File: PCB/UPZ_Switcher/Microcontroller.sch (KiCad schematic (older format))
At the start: 9 parts, among them IC1 MAX232ECPE+, J1 5747844-6

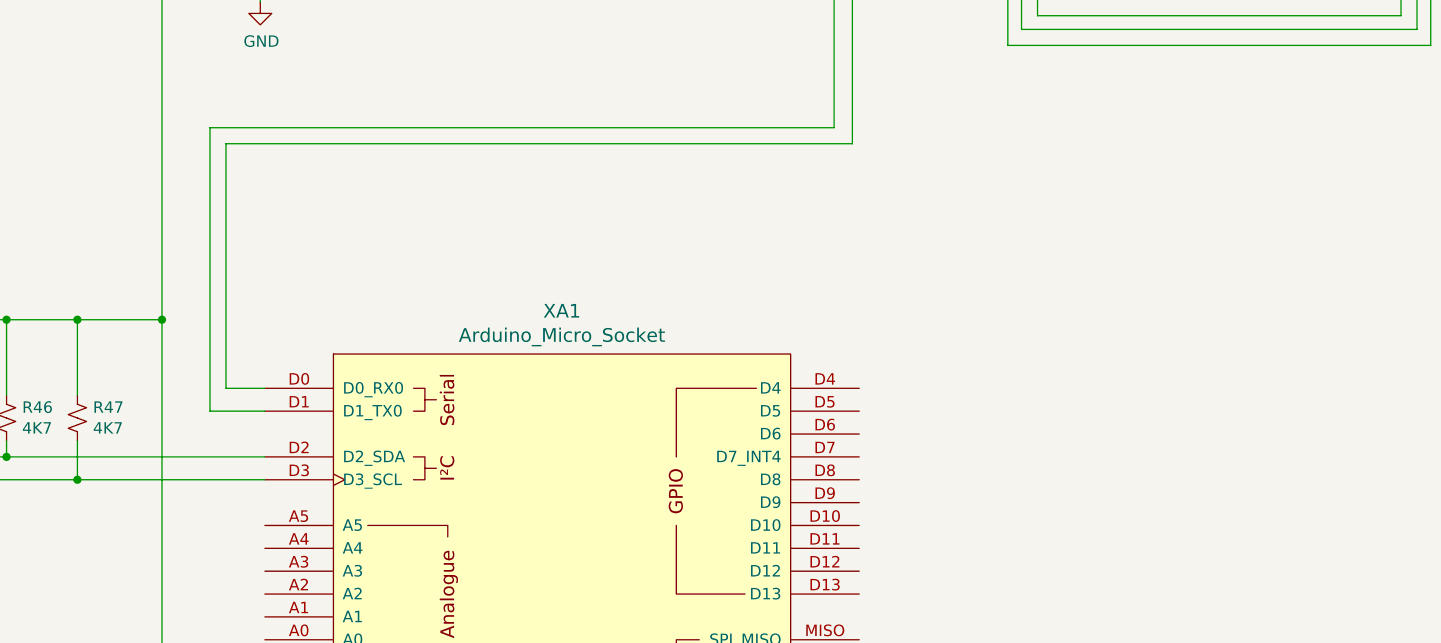
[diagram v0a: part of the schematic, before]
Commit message: Updated schematic, PSU added + draft program
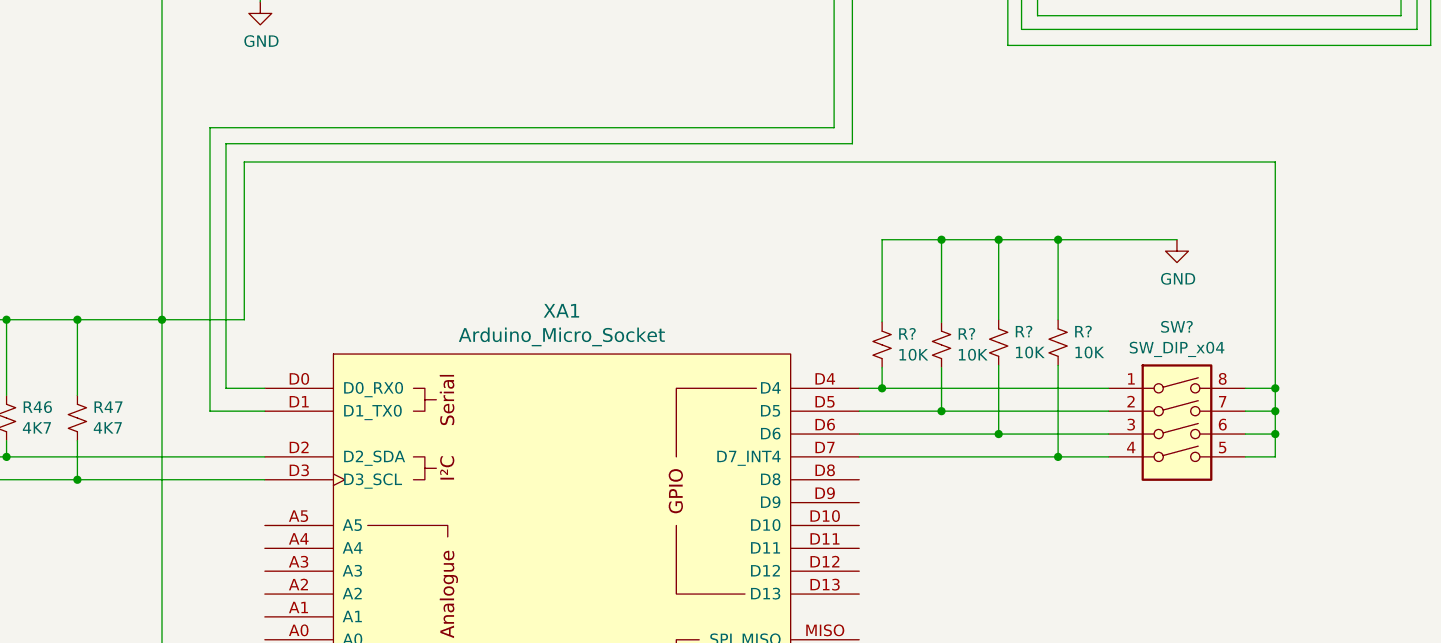
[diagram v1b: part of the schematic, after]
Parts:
- added R? (x4): 10K, Resistor_SMD:R_1206_3216Metric, symbol Device:R_Small_US
- added SW?: SW_DIP_x04, Button_Switch_THT:SW_DIP_SPSTx04_Slide_9.78x12.34mm_W7.62mm_P2.54mm, symbol Switch:SW_DIP_x04
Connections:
- wire segments 68 -> 99
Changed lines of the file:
@@
 $Descr A3 16535 11693
 encoding utf-8
-Sheet 3 6
+Sheet 3 5
 Title "Microcontroller Board"
 Date "2021-02-28"
@@
 Wire Wire Line
 	10450 1540 10590 1540
+$Comp
+L Switch:SW_DIP_x04 SW?
+U 1 1 603D5AFB
+P 10800 4200
+F 0 "SW?" H 10800 4667 50  0000 C CNN
+F 1 "SW_DIP_x04" H 10800 4576 50  0000 C CNN
+F 2 "Button_Switch_THT:SW_DIP_SPSTx04_Slide_9.78x12.34mm_W7.62mm_P2.54mm" H 10800 4200 50  0001 C CNN
+F 3 "~" H 10800 4200 50  0001 C CNN
+	1    10800 4200
+	1    0    0    -1
+$EndComp
+Wire Wire Line
+	6360 3700 6720 3700
+Wire Wire Line
+	6720 3700 6720 3010
+Wire Wire Line
+	11230 4000 11100 4000
+Wire Wire Line
+	11100 4100 11230 4100
+Connection ~ 11230 4000
+Wire Wire Line
+	11100 4200 11230 4200
+Wire Wire Line
+	11230 4000 11230 4100
+Connection ~ 11230 4100
+Wire Wire Line
+	11230 4100 11230 4200
+Wire Wire Line
+	11100 4300 11230 4300
+Wire Wire Line
+	11230 4300 11230 4200
+Connection ~ 11230 4200
+Wire Wire Line
+	11230 3010 11230 4000
+$Comp
+L Device:R_Small_US R?
+U 1 1 603E88E2
+P 9510 3810
+F 0 "R?" H 9578 3856 50  0000 L CNN
+F 1 "10K" H 9578 3765 50  0000 L CNN
+F 2 "Resistor_SMD:R_1206_3216Metric" H 9510 3810 50  0001 C CNN
+F 3 "~" H 9510 3810 50  0001 C CNN
+	1    9510 3810
+	1    0    0    -1
+$EndComp
+$Comp
+L Device:R_Small_US R?
+U 1 1 603EE6CE
+P 9770 3810
+F 0 "R?" H 9838 3856 50  0000 L CNN
+F 1 "10K" H 9838 3765 50  0000 L CNN
+F 2 "Resistor_SMD:R_1206_3216Metric" H 9770 3810 50  0001 C CNN
+F 3 "~" H 9770 3810 50  0001 C CNN
+	1    9770 3810
+	1    0    0    -1
+$EndComp
+$Comp
+L Device:R_Small_US R?
+U 1 1 603FFE72
+P 10020 3800
+F 0 "R?" H 10088 3846 50  0000 L CNN
+F 1 "10K" H 10088 3755 50  0000 L CNN
+F 2 "Resistor_SMD:R_1206_3216Metric" H 10020 3800 50  0001 C CNN
+F 3 "~" H 10020 3800 50  0001 C CNN
+	1    10020 3800
+	1    0    0    -1
+$EndComp
+$Comp
+L Device:R_Small_US R?
+U 1 1 603FFE7C
+P 10280 3800
+F 0 "R?" H 10348 3846 50  0000 L CNN
+F 1 "10K" H 10348 3755 50  0000 L CNN
+F 2 "Resistor_SMD:R_1206_3216Metric" H 10280 3800 50  0001 C CNN
+F 3 "~" H 10280 3800 50  0001 C CNN
+	1    10280 3800
+	1    0    0    -1
+$EndComp
+Wire Wire Line
+	6720 3010 11230 3010
+Wire Wire Line
+	9410 4000 9510 4000
+Wire Wire Line
+	9410 4100 9770 4100
+Wire Wire Line
+	9410 4200 10020 4200
+Wire Wire Line
+	9410 4300 10280 4300
+Wire Wire Line
+	10280 3900 10280 4300
+Connection ~ 10280 4300
+Wire Wire Line
+	10280 4300 10500 4300
+Wire Wire Line
+	10020 3900 10020 4200
+Connection ~ 10020 4200
+Wire Wire Line
+	10020 4200 10500 4200
+Wire Wire Line
+	9770 3910 9770 4100
+Connection ~ 9770 4100
+Wire Wire Line
+	9770 4100 10500 4100
+Wire Wire Line
+	9510 3910 9510 4000
+Connection ~ 9510 4000
+Wire Wire Line
+	9510 4000 10500 4000
+$Comp
+L power:GND #PWR?
+U 1 1 604268ED
+P 10800 3350
+F 0 "#PWR?" H 10800 3100 50  0001 C CNN
+F 1 "GND" H 10805 3177 50  0000 C CNN
+F 2 "" H 10800 3350 50  0001 C CNN
+F 3 "" H 10800 3350 50  0001 C CNN
+	1    10800 3350
+	1    0    0    -1
+$EndComp
+Wire Wire Line
+	9510 3350 9770 3350
+Wire Wire Line
+	9510 3350 9510 3710
+Wire Wire Line
+	9770 3710 9770 3350
+Connection ~ 9770 3350
+Wire Wire Line
+	9770 3350 10020 3350
+Wire Wire Line
+	10020 3700 10020 3350
+Connection ~ 10020 3350
+Wire Wire Line
+	10020 3350 10280 3350
+Wire Wire Line
+	10280 3700 10280 3350
+Connection ~ 10280 3350
+Wire Wire Line
+	10280 3350 10800 3350
 $EndSCHEMATC

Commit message: Started PCB design
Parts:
- added R1, R2, R3: 10K, Resistor_SMD:R_1206_3216Metric, symbol Device:R_Small_US
- added R5: 20K, Resistor_SMD:R_1206_3216Metric, symbol Device:R_Small_US
- added R7: 40K, Resistor_SMD:R_1206_3216Metric, symbol Device:R_Small_US
- added R9: 80K, Resistor_SMD:R_1206_3216Metric, symbol Device:R_Small_US
- added SW1: SW_DIP_x04, Button_Switch_THT:SW_DIP_SPSTx04_Slide_9.78x12.34mm_W7.62mm_P2.54mm, symbol Switch:SW_DIP_x04
- R10: renamed from R?; value 10K -> 80K
- R6: renamed from R?; value 10K -> 20K
- R8: renamed from R?; value 10K -> 40K
- gave numbers to parts that had none: 2
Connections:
- wire segments 99 -> 122
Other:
- note added: "Input \nSwitcher \nDIP Address"
- note added: "Output \nSwitcher \nDIP Address"
- moved on the sheet: R10, R4, R6, R8, SW2

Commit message: updated phantom design + MCU board
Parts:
- removed J1: 5747844-6, 57478446, symbol BVKSound:5747844-6
- added J1: FROM PSU, BVKSound:71918-110LF, symbol BVKSound:71918-110LF
- added J2: TO RELAY, BVKSound:71918-110LF, symbol BVKSound:71918-110LF
- added J3: FROM PREVIOUS, Connector_Dsub:DSUB-9_Female_Horizontal_P2.77x2.84mm_EdgePinOffset4.94mm_Housed_MountingHolesOffset7.48mm, symbol Connector:DB9_Female
- added J4: TO NEXT, Connector_Dsub:DSUB-9_Male_Horizontal_P2.77x2.84mm_EdgePinOffset4.94mm_Housed_MountingHolesOffset7.48mm, symbol Connector:DB9_Male
- C19, C20, C21, C22: footprint (none) -> Capacitor_THT:CP_Radial_D5.0mm_P2.50mm
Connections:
- wire segments 122 -> 146
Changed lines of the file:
@@
 $Descr A3 16535 11693
 encoding utf-8
-Sheet 1 6
+Sheet 1 1
 Title "Microcontroller Board"
 Date "2021-02-28"
@@
 	1    0    0    -1
 $EndComp
-$Comp
-L BVKSound:5747844-6 J1
-U 1 1 63464424
-P 11090 1140
-F 0 "J1" V 10909 1140 50  0000 C CNN
-F 1 "5747844-6" V 11000 1140 50  0000 C CNN
-F 2 "57478446" H 11940 1440 50  0001 L CNN
-F 3 "http://www.te.com/commerce/DocumentDelivery/DDEController?Action=showdoc&DocId=Customer+Drawing%7F5747844%7FP%7Fpdf%7FEnglish%7FENG_CD_5747844_P.pdf%7F5747844-6" H 11940 1340 50  0001 L CNN
-F 4 "9 way r/a PCB D socket w/screw lock,6A" H 11940 1240 50  0001 L CNN "Description"
-F 5 "12" H 11940 1140 50  0001 L CNN "Height"
-F 6 "TE Connectivity" H 11940 1040 50  0001 L CNN "Manufacturer_Name"
-F 7 "5747844-6" H 11940 940 50  0001 L CNN "Manufacturer_Part_Number"
-F 8 "571-5747844-6" H 11940 840 50  0001 L CNN "Mouser Part Number"
-F 9 "https://www.mouser.co.uk/ProductDetail/TE-Connectivity/5747844-6?qs=x6EjVpvqMVNBaI3EeeZZVw%3D%3D" H 11940 740 50  0001 L CNN "Mouser Price/Stock"
-F 10 "5747844-6" H 11940 640 50  0001 L CNN "Arrow Part Number"
-F 11 "https://www.arrow.com/en/products/5747844-6/te-connectivity" H 11940 540 50  0001 L CNN "Arrow Price/Stock"
-	1    11090 1140
-	0    1    1    0
-$EndComp
 Wire Wire Line
 	8790 1680 10120 1680
 Wire Wire Line
 	10120 1680 10120 2430
-Wire Wire Line
-	10120 2430 11850 2430
-Wire Wire Line
-	11850 2430 11850 1740
-Wire Wire Line
-	11850 1740 11590 1740
-Wire Wire Line
-	11590 1640 11910 1640
-Wire Wire Line
-	11910 1640 11910 2500
-Wire Wire Line
-	11910 2500 10060 2500
 Wire Wire Line
 	10060 2500 10060 1780
@@
 F 0 "C19" H 6878 1626 50  0000 L CNN
 F 1 "1uF" H 6878 1535 50  0000 L CNN
-F 2 "" H 6790 1580 50  0001 C CNN
+F 2 "Capacitor_THT:CP_Radial_D5.0mm_P2.50mm" H 6790 1580 50  0001 C CNN
 F 3 "~" H 6790 1580 50  0001 C CNN
 	1    6790 1580
@@
 F 0 "C22" H 7338 1336 50  0000 L CNN
 F 1 "1uF" H 7338 1245 50  0000 L CNN
-F 2 "" H 7250 1290 50  0001 C CNN
+F 2 "Capacitor_THT:CP_Radial_D5.0mm_P2.50mm" H 7250 1290 50  0001 C CNN
 F 3 "~" H 7250 1290 50  0001 C CNN
 	1    7250 1290
@@
 F 0 "C20" H 6878 1926 50  0000 L CNN
 F 1 "1uF" H 6878 1835 50  0000 L CNN
-F 2 "" H 6790 1880 50  0001 C CNN
+F 2 "Capacitor_THT:CP_Radial_D5.0mm_P2.50mm" H 6790 1880 50  0001 C CNN
 F 3 "~" H 6790 1880 50  0001 C CNN
 	1    6790 1880
@@
 F 0 "C21" H 6702 2114 50  0000 R CNN
 F 1 "1uF" H 6702 2205 50  0000 R CNN
-F 2 "" H 6790 2160 50  0001 C CNN
+F 2 "Capacitor_THT:CP_Radial_D5.0mm_P2.50mm" H 6790 2160 50  0001 C CNN
 F 3 "~" H 6790 2160 50  0001 C CNN
 	1    6790 2160
@@
 Wire Wire Line
 	6790 2310 6790 2260
-$Comp
-L power:GND #PWR0126
-U 1 1 6348982D
-P 12220 1440
-F 0 "#PWR0126" H 12220 1190 50  0001 C CNN
-F 1 "GND" H 12225 1267 50  0000 C CNN
-F 2 "" H 12220 1440 50  0001 C CNN
-F 3 "" H 12220 1440 50  0001 C CNN
-	1    12220 1440
-	1    0    0    -1
-$EndComp
-Wire Wire Line
-	11590 1440 12220 1440
-Wire Wire Line
-	11590 1540 11780 1540
-Wire Wire Line
-	11780 1540 11780 2370
-Wire Wire Line
-	11780 2370 10190 2370
-Wire Wire Line
-	10190 2370 10190 1740
-Wire Wire Line
-	10190 1740 10590 1740
-Wire Wire Line
-	10590 1640 10450 1640
-Wire Wire Line
-	10450 1640 10450 1540
-Wire Wire Line
-	10450 1540 10590 1540
 $Comp
 L Switch:SW_DIP_x04 SW2
@@
 Wire Wire Line
 	8790 1980 9820 1980
+$Comp
+L Connector:DB9_Female J3
+U 1 1 604F5662
+P 11240 3140
+F 0 "J3" H 11420 3186 50  0000 L CNN
+F 1 "FROM PREVIOUS" H 11420 3095 50  0000 L CNN
+F 2 "Connector_Dsub:DSUB-9_Female_Horizontal_P2.77x2.84mm_EdgePinOffset4.94mm_Housed_MountingHolesOffset7.48mm" H 11240 3140 50  0001 C CNN
+F 3 " ~" H 11240 3140 50  0001 C CNN
+	1    11240 3140
+	1    0    0    -1
+$EndComp
+$Comp
+L Connector:DB9_Male J4
+U 1 1 604F7554
+P 13410 3100
+F 0 "J4" H 13590 3146 50  0000 L CNN
+F 1 "TO NEXT" H 13590 3055 50  0000 L CNN
+F 2 "Connector_Dsub:DSUB-9_Male_Horizontal_P2.77x2.84mm_EdgePinOffset4.94mm_Housed_MountingHolesOffset7.48mm" H 13410 3100 50  0001 C CNN
+F 3 " ~" H 13410 3100 50  0001 C CNN
+	1    13410 3100
+	1    0    0    -1
+$EndComp
+Wire Wire Line
+	10940 3040 10860 3040
+Wire Wire Line
+	10860 3040 10860 3240
+Wire Wire Line
+	10860 3240 10940 3240
+Wire Wire Line
+	13110 3000 13030 3000
+Wire Wire Line
+	13030 3000 13030 3200
+Wire Wire Line
+	13030 3200 13110 3200
+$Comp
+L power:GND #PWR0103
+U 1 1 60503CD7
+P 10870 3640
+F 0 "#PWR0103" H 10870 3390 50  0001 C CNN
+F 1 "GND" H 10875 3467 50  0000 C CNN
+F 2 "" H 10870 3640 50  0001 C CNN
+F 3 "" H 10870 3640 50  0001 C CNN
+	1    10870 3640
+	1    0    0    -1
+$EndComp
+Wire Wire Line
+	10870 3640 10870 3540
+Wire Wire Line
+	10870 3540 10940 3540
+$Comp
+L power:GND #PWR0104
+U 1 1 6051424F
+P 12880 3640
+F 0 "#PWR0104" H 12880 3390 50  0001 C CNN
+F 1 "GND" H 12885 3467 50  0000 C CNN
+F 2 "" H 12880 3640 50  0001 C CNN
+F 3 "" H 12880 3640 50  0001 C CNN
+	1    12880 3640
+	1    0    0    -1
+$EndComp
+Wire Wire Line
+	12880 2700 13110 2700
+Wire Wire Line
+	12880 2700 12880 3640
+Wire Wire Line
+	10940 2840 10710 2840
+Wire Wire Line
+	10710 2840 10710 3340
+Wire Wire Line
+	10710 3340 10940 3340
+Wire Wire Line
+	10120 2430 10120 2940
+Wire Wire Line
+	10120 2940 10940 2940
+Connection ~ 10120 2430
+Wire Wire Line
+	10060 2500 10060 3140
+Wire Wire Line
+	10060 3140 10940 3140
+Connection ~ 10060 2500
+Wire Wire Line
+	12310 2500 12310 3300
+Wire Wire Line
+	12310 3300 13110 3300
+Wire Wire Line
+	12420 2430 12420 3100
+Wire Wire Line
+	12420 3100 13110 3100
+Wire Wire Line
+	10060 2500 12310 2500
+Wire Wire Line
+	10120 2430 12420 2430
+$Comp
+L BVKSound:71918-110LF J2
+U 1 1 6055C082
+P 6910 6550
+F 0 "J2" H 7438 6053 60  0000 L CNN
+F 1 "TO RELAY" H 7438 5947 60  0000 L CNN
+F 2 "BVKSound:71918-110LF" H 7310 5890 60  0001 C CNN
+F 3 "" H 6910 6550 60  0000 C CNN
+	1    6910 6550
+	1    0    0    -1
+$EndComp
+Wire Wire Line
+	5680 6550 6910 6550
+Wire Wire Line
+	5680 4300 5680 6550
+Wire Wire Line
+	5990 4400 5990 6650
+Wire Wire Line
+	5990 6650 6910 6650
+Wire Wire Line
+	6360 5700 6360 6750
+Wire Wire Line
+	6360 6750 6910 6750
+Connection ~ 6360 5700
+Wire Wire Line
+	6590 5500 6590 6950
+Wire Wire Line
+	6590 6950 6910 6950
+Connection ~ 6590 5500
+$Comp
+L BVKSound:71918-110LF J1
+U 1 1 60579496
+P 5190 6550
+F 0 "J1" H 5830 6100 60  0000 C CNN
+F 1 "FROM PSU" H 5960 5980 60  0000 C CNN
+F 2 "BVKSound:71918-110LF" H 5590 5890 60  0001 C CNN
+F 3 "" H 5190 6550 60  0000 C CNN
+	1    5190 6550
+	-1   0    0    -1
+$EndComp
+Wire Wire Line
+	5190 7450 6910 7450
+Wire Wire Line
+	6910 7350 5190 7350
+Wire Wire Line
+	5190 7250 6910 7250
+Wire Wire Line
+	5190 7150 6910 7150
+Wire Wire Line
+	5190 7050 6910 7050
+Wire Wire Line
+	5190 6950 6590 6950
+Connection ~ 6590 6950
+Wire Wire Line
+	5190 6750 6360 6750
+Wire Wire Line
+	6360 6750 6360 6740
+Connection ~ 6360 6750
 $EndSCHEMATC

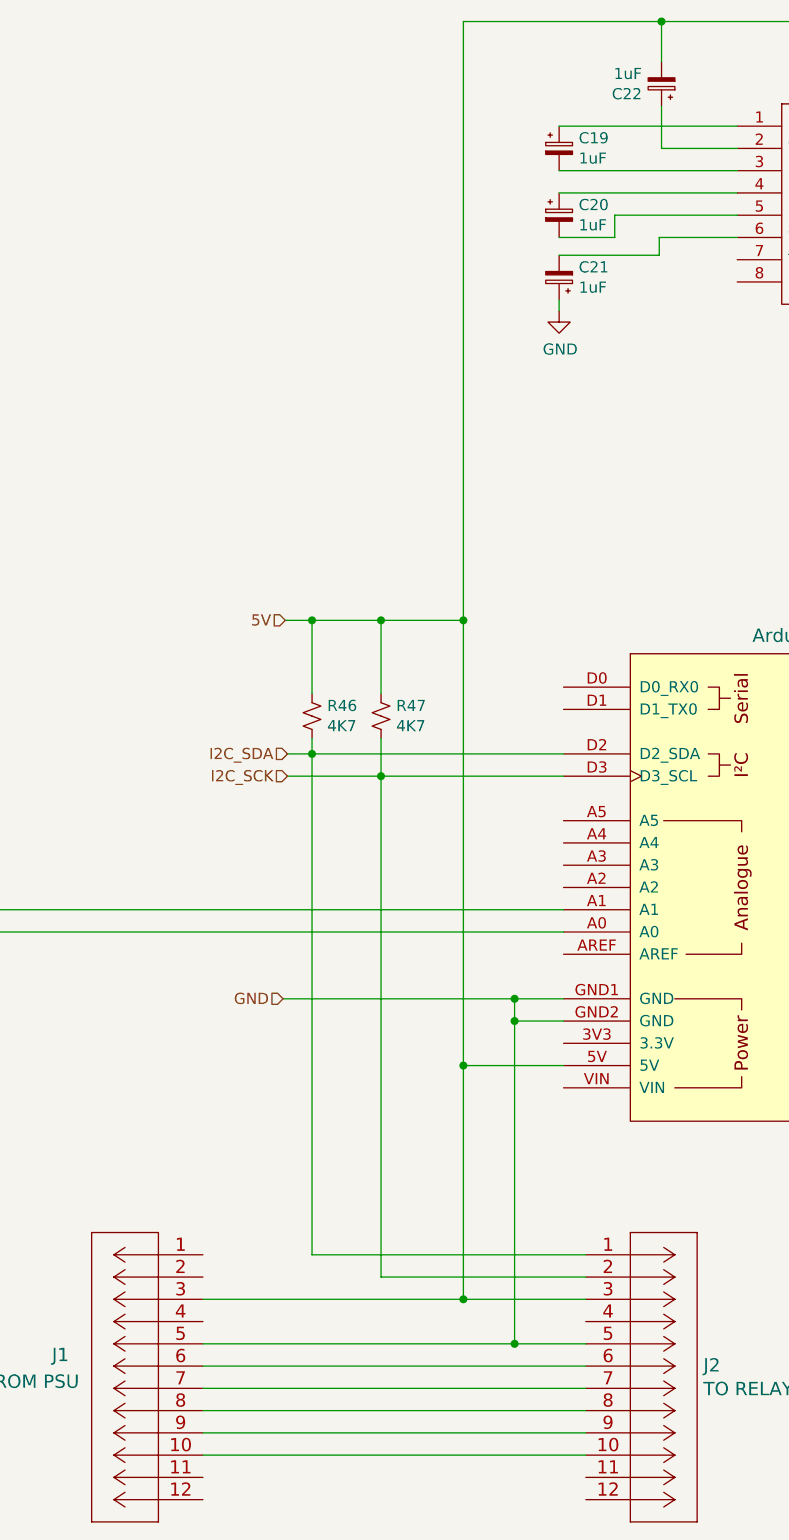
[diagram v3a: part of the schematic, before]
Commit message: update on power supply
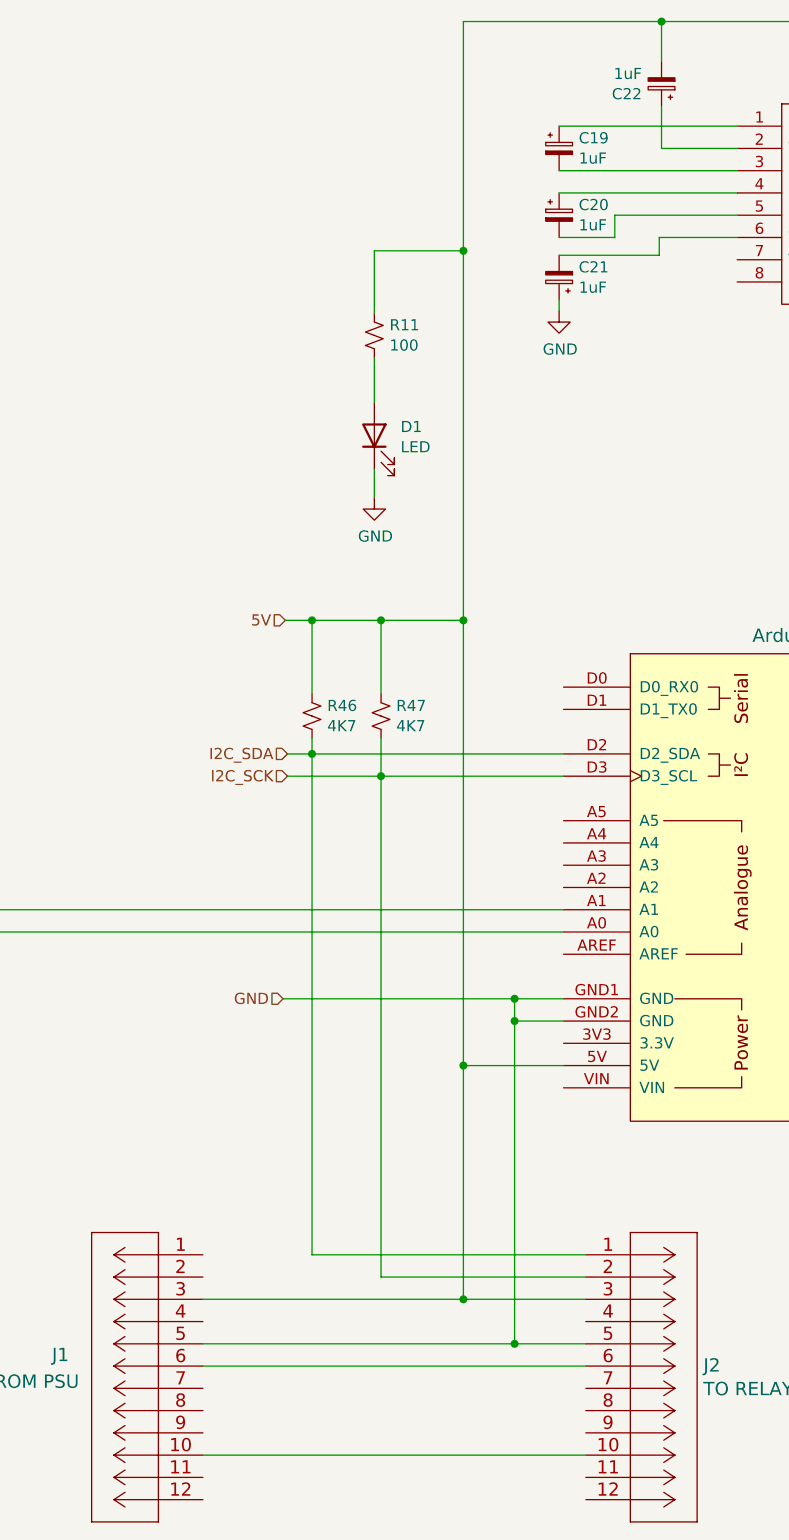
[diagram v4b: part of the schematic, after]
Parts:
- added D1: LED, LED_THT:LED_D3.0mm, symbol Device:LED
- added R11: 100, Resistor_SMD:R_1206_3216Metric, symbol Device:R_Small_US
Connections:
- net 5V: now also R11.1
- net GND: now also D1.1 (K)
- net at J2.7: no longer J1.7
- net at J2.8: no longer J1.8
- net at J2.9: no longer J1.9
- new net: D1.2 (A), R11.2
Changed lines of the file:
@@
 	10060 1780 8790 1780
 Wire Wire Line
-	6360 3700 6360 1010
+	6360 3700 6360 2040
 Wire Wire Line
 	6360 1010 7250 1010
@@
 	5190 7450 6910 7450
 Wire Wire Line
-	6910 7350 5190 7350
-Wire Wire Line
-	5190 7250 6910 7250
-Wire Wire Line
-	5190 7150 6910 7150
-Wire Wire Line
 	5190 7050 6910 7050
 Wire Wire Line
@@
 	6360 6750 6360 6740
 Connection ~ 6360 6750
+$Comp
+L power:GND #PWR0105
+U 1 1 604FFC6D
+P 5960 3150
+F 0 "#PWR0105" H 5960 2900 50  0001 C CNN
+F 1 "GND" H 5965 2977 50  0000 C CNN
+F 2 "" H 5960 3150 50  0001 C CNN
+F 3 "" H 5960 3150 50  0001 C CNN
+	1    5960 3150
+	1    0    0    -1
+$EndComp
+$Comp
+L Device:LED D1
+U 1 1 6050ECF1
+P 5960 2870
+F 0 "D1" V 5999 2752 50  0000 R CNN
+F 1 "LED" V 5908 2752 50  0000 R CNN
+F 2 "LED_THT:LED_D3.0mm" H 5960 2870 50  0001 C CNN
+F 3 "~" H 5960 2870 50  0001 C CNN
+	1    5960 2870
+	0    -1   -1   0
+$EndComp
+$Comp
+L Device:R_Small_US R11
+U 1 1 6050F358
+P 5960 2420
+F 0 "R11" H 6028 2466 50  0000 L CNN
+F 1 "100" H 6028 2375 50  0000 L CNN
+F 2 "Resistor_SMD:R_1206_3216Metric" H 5960 2420 50  0001 C CNN
+F 3 "~" H 5960 2420 50  0001 C CNN
+	1    5960 2420
+	1    0    0    -1
+$EndComp
+Wire Wire Line
+	5960 3150 5960 3020
+Wire Wire Line
+	5960 2720 5960 2520
+Wire Wire Line
+	5960 2320 5960 2040
+Wire Wire Line
+	5960 2040 6360 2040
+Connection ~ 6360 2040
+Wire Wire Line
+	6360 2040 6360 1010
 $EndSCHEMATC
